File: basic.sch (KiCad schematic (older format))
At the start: 5 parts, among them J5 Conn_02x02_Top_Bottom, X1 dummy, X2 dummy

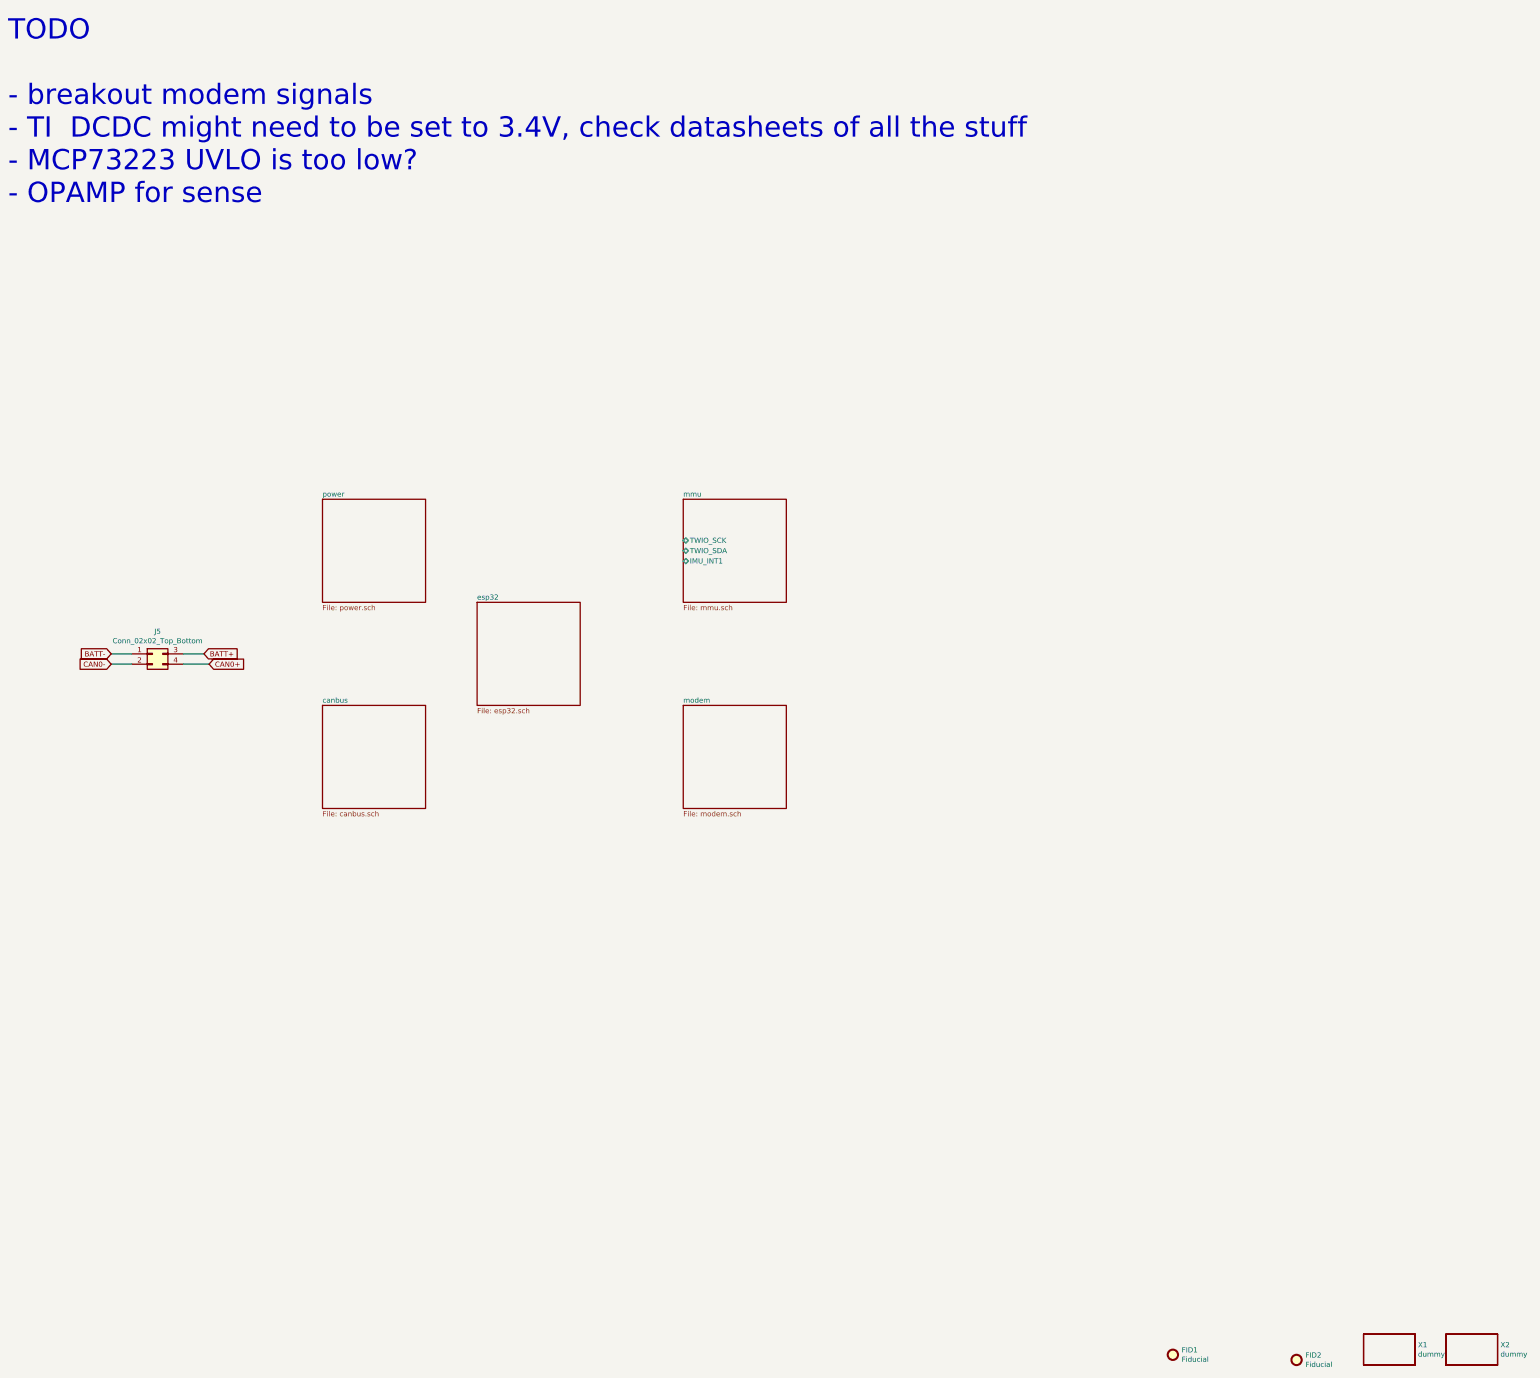
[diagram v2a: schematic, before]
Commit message: Esp32 & Canbus Sch. edited.
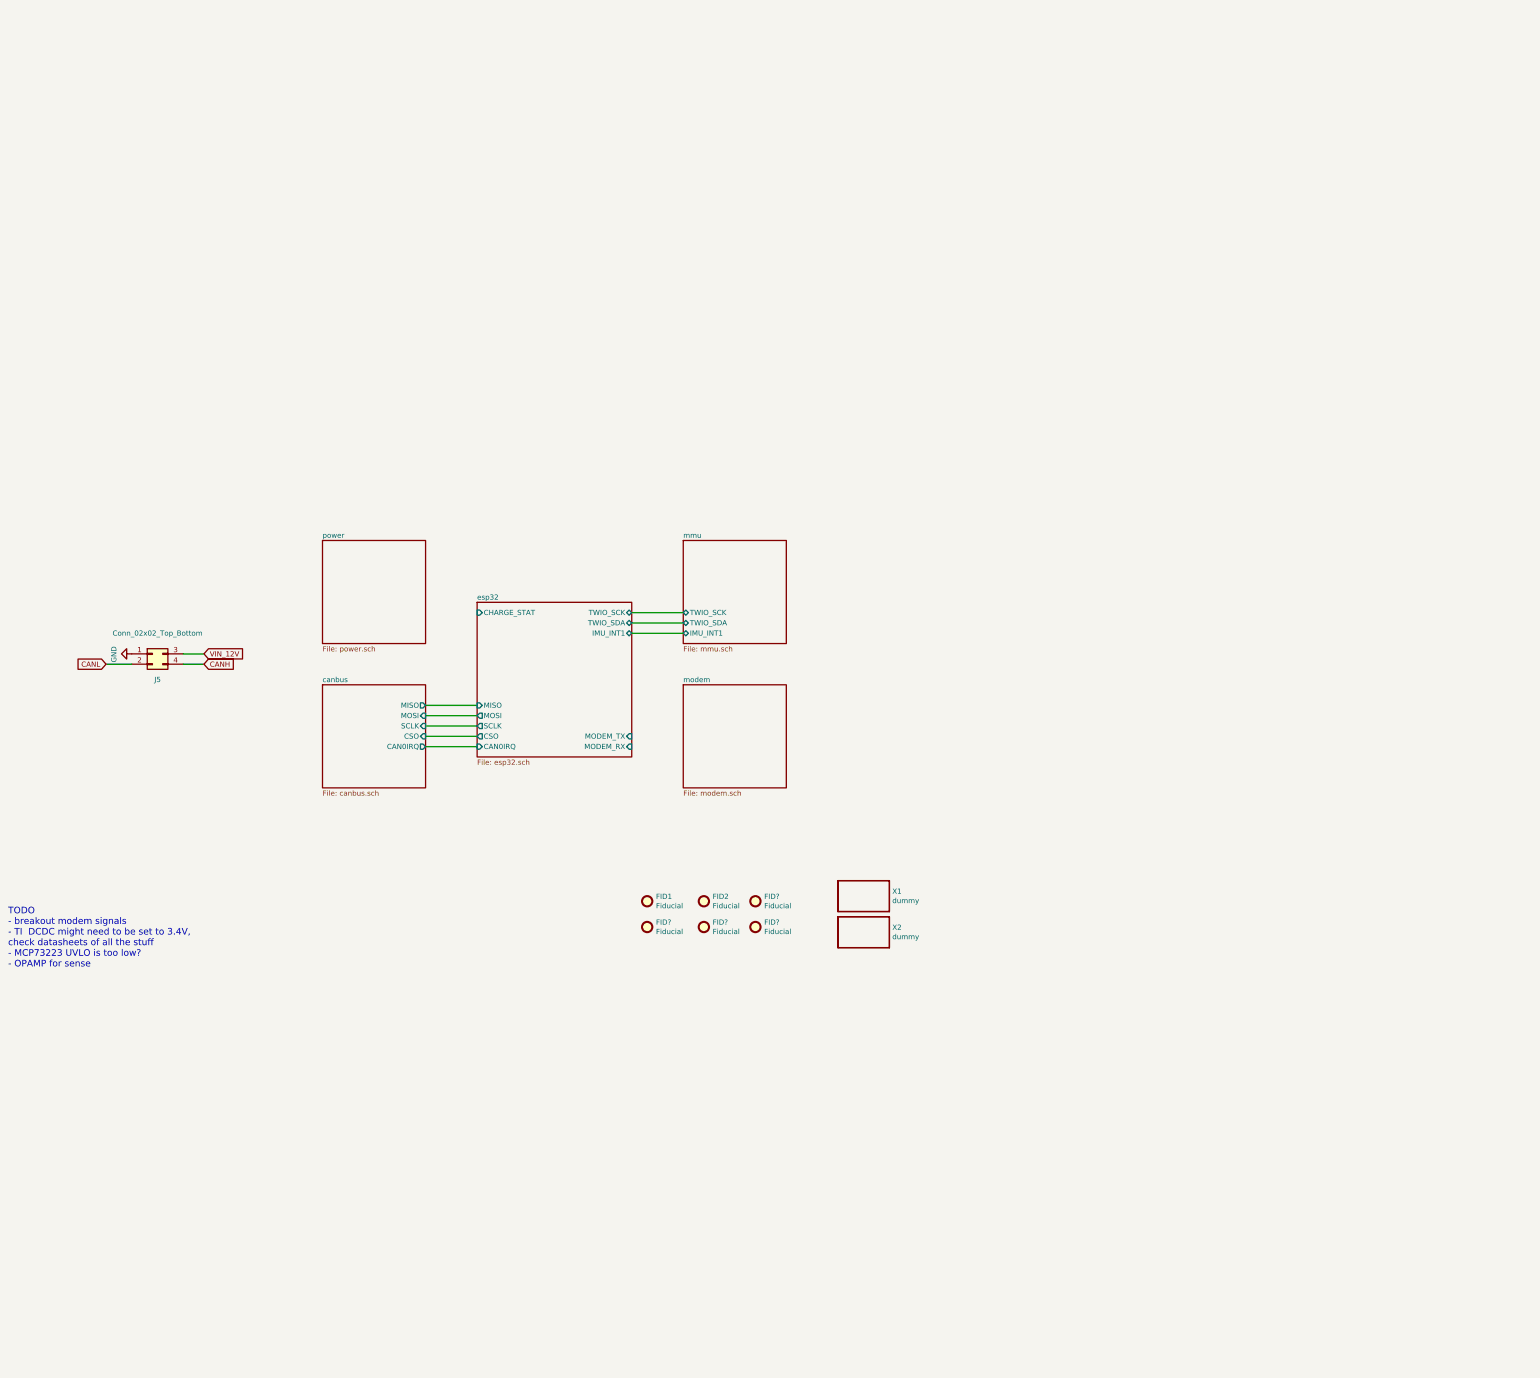
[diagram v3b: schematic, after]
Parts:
- added FID? (x4): Fiducial, Aesthetics:FIDUCIAL-1X2, symbol Mechanical:Fiducial
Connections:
- net BATT+ renamed VIN_12V
- net BATT- renamed GND
- net CAN0+ renamed CANH
- net CAN0- renamed CANL
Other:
- note added: "TODO\n- breakout modem signals\n- TI DCDC might need to be set to 3.4V, \ncheck datasheets of all the stuff\n- MCP73223 UVLO is too low?\n- OPAMP for sense"
- note removed: "TODO\n\n- breakout modem signals\n- TI DCDC might need to be set to 3.4V, check datasheets of all the stuff\n- MCP73223 UVLO is too low?\n- OPAMP for sense"
- moved on the sheet: FID1, FID2, X1, X2
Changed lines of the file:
@@
 L Mechanical:Fiducial FID1
 U 1 1 5E789BF2
-P 12250 10300
-F 0 "FID1" H 12335 10346 50  0000 L CNN
-F 1 "Fiducial" H 12335 10255 50  0000 L CNN
-F 2 "Aesthetics:FIDUCIAL-1X2" H 12250 10300 50  0001 C CNN
-F 3 "~" H 12250 10300 50  0001 C CNN
-	1    12250 10300
+P 7150 5900
+F 0 "FID1" H 7235 5946 50  0000 L CNN
+F 1 "Fiducial" H 7235 5855 50  0000 L CNN
+F 2 "Aesthetics:FIDUCIAL-1X2" H 7150 5900 50  0001 C CNN
+F 3 "~" H 7150 5900 50  0001 C CNN
+	1    7150 5900
 	1    0    0    -1
 $EndComp
 Wire Wire Line
 	2850 3500 2650 3500
-Wire Wire Line
-	1950 3600 2150 3600
-Text GLabel 2900 3600 2    50   Input ~ 0
-CAN0+
-Wire Wire Line
-	2650 3600 2900 3600
 $Comp
 L Mechanical:Fiducial FID2
 U 1 1 5E789C24
-P 13450 10350
-F 0 "FID2" H 13535 10396 50  0000 L CNN
-F 1 "Fiducial" H 13535 10305 50  0000 L CNN
-F 2 "Aesthetics:FIDUCIAL-1X2" H 13450 10350 50  0001 C CNN
-F 3 "~" H 13450 10350 50  0001 C CNN
-	1    13450 10350
+P 7700 5900
+F 0 "FID2" H 7785 5946 50  0000 L CNN
+F 1 "Fiducial" H 7785 5855 50  0000 L CNN
+F 2 "Aesthetics:FIDUCIAL-1X2" H 7700 5900 50  0001 C CNN
+F 3 "~" H 7700 5900 50  0001 C CNN
+	1    7700 5900
 	1    0    0    -1
 $EndComp
-Wire Wire Line
-	1950 3500 2150 3500
 Text GLabel 2850 3500 2    50   Input ~ 0
-BATT+
+VIN_12V
 $Comp
 L Connector_Generic:Conn_02x02_Top_Bottom J5
 U 1 1 5E789BF0
 P 2350 3500
-F 0 "J5" H 2400 3717 50  0000 C CNN
-F 1 "Conn_02x02_Top_Bottom" H 2400 3626 50  0000 C CNN
+F 0 "J5" H 2400 3250 50  0000 C CNN
+F 1 "Conn_02x02_Top_Bottom" H 2400 3700 50  0000 C CNN
 F 2 "Connector_Molex:Molex_Micro-Fit_3.0_43045-0400_2x02_P3.00mm_Horizontal" H 2350 3500 50  0001 C CNN
 F 3 "~" H 2350 3500 50  0001 C CNN
@@
 	1    0    0    -1
 $EndComp
-Text GLabel 1950 3500 0    50   Input ~ 0
-BATT-
-Text GLabel 1950 3600 0    50   Input ~ 0
-CAN0-
-Text Notes 950  -850 0    197  ~ 0
-TODO\n\n- breakout modem signals\n- TI  DCDC might need to be set to 3.4V, check datasheets of all the stuff\n- MCP73223 UVLO is too low?\n- OPAMP for sense
+Text Notes 950  6550 0    64   ~ 0
+TODO\n- breakout modem signals\n- TI  DCDC might need to be set to 3.4V, \ncheck datasheets of all the stuff\n- MCP73223 UVLO is too low?\n- OPAMP for sense
 $Sheet
-S 4000 2000 1000 1000
+S 4000 2400 1000 1000
 U 60856F71
 F0 "power" 50
@@
 L aep:dummy X1
 U 1 1 6202ADD4
-P 14350 10250
-F 0 "X1" H 14628 10296 50  0000 L CNN
-F 1 "dummy" H 14628 10205 50  0000 L CNN
-F 2 "aep:WEEE-Logo_2.1x3mm_SilkScreen" H 14350 10250 50  0001 C CNN
-F 3 "" H 14350 10250 50  0001 C CNN
-	1    14350 10250
+P 9250 5850
+F 0 "X1" H 9528 5896 50  0000 L CNN
+F 1 "dummy" H 9528 5805 50  0000 L CNN
+F 2 "aep:WEEE-Logo_2.1x3mm_SilkScreen" H 9250 5850 50  0001 C CNN
+F 3 "" H 9250 5850 50  0001 C CNN
+	1    9250 5850
 	1    0    0    -1
 $EndComp
@@
 L aep:dummy X2
 U 1 1 6202DDC3
-P 15150 10250
-F 0 "X2" H 15428 10296 50  0000 L CNN
-F 1 "dummy" H 15428 10205 50  0000 L CNN
-F 2 "Aesthetics:OSHW-LOGO-S" H 15150 10250 50  0001 C CNN
-F 3 "" H 15150 10250 50  0001 C CNN
-	1    15150 10250
+P 9250 6200
+F 0 "X2" H 9528 6246 50  0000 L CNN
+F 1 "dummy" H 9528 6155 50  0000 L CNN
+F 2 "Aesthetics:OSHW-LOGO-S" H 9250 6200 50  0001 C CNN
+F 3 "" H 9250 6200 50  0001 C CNN
+	1    9250 6200
 	1    0    0    -1
 $EndComp
 $Sheet
-S 4000 4000 1000 1000
+S 4000 3800 1000 1000
 U 603BB897
 F0 "canbus" 50
 F1 "canbus.sch" 50
+F2 "MISO" O R 5000 4000 50
+F3 "MOSI" I R 5000 4100 50
+F4 "SCLK" I R 5000 4200 50
+F5 "CSO" I R 5000 4300 50
+F6 "CAN0IRQ" O R 5000 4400 50
 $EndSheet
 $Sheet
-S 7500 4000 1000 1000
+S 7500 3800 1000 1000
 U 6055B0F2
 F0 "modem" 50
@@
 $EndSheet
 $Sheet
-S 7500 2000 1000 1000
+S 7500 2400 1000 1000
 U 606146CD
 F0 "mmu" 50
 F1 "mmu.sch" 50
-F2 "TWIO_SCK" B L 7500 2400 50
-F3 "TWIO_SDA" B L 7500 2500 50
-F4 "IMU_INT1" B L 7500 2600 50
+F2 "TWIO_SCK" B L 7500 3100 50
+F3 "TWIO_SDA" B L 7500 3200 50
+F4 "IMU_INT1" B L 7500 3300 50
 $EndSheet
+Wire Wire Line
+	7000 3100 7500 3100
+Wire Wire Line
+	7000 3200 7500 3200
+Wire Wire Line
+	7000 3300 7500 3300
+Wire Wire Line
+	5500 4000 5000 4000
+Wire Wire Line
+	5000 4100 5500 4100
+Wire Wire Line
+	5500 4200 5000 4200
+Wire Wire Line
+	5000 4300 5500 4300
+Wire Wire Line
+	5500 4400 5000 4400
+Text GLabel 2850 3600 2    50   Input ~ 0
+CANH
+Text GLabel 1900 3600 0    50   Input ~ 0
+CANL
+Wire Wire Line
+	2850 3600 2650 3600
 $Sheet
-S 5500 3000 1000 1000
+S 5500 3000 1500 1500
 U 603B75FA
 F0 "esp32" 50
 F1 "esp32.sch" 50
+F2 "TWIO_SCK" B R 7000 3100 50
+F3 "TWIO_SDA" B R 7000 3200 50
+F4 "IMU_INT1" B R 7000 3300 50
+F5 "MODEM_TX" I R 7000 4300 50
+F6 "MODEM_RX" I R 7000 4400 50
+F7 "CHARGE_STAT" I L 5500 3100 50
+F8 "CAN0IRQ" I L 5500 4400 50
+F9 "MISO" I L 5500 4000 50
+F10 "MOSI" O L 5500 4100 50
+F11 "SCLK" O L 5500 4200 50
+F12 "CSO" O L 5500 4300 50
 $EndSheet
+$Comp
+L Mechanical:Fiducial FID?
+U 1 1 605974C2
+P 8200 5900
+F 0 "FID?" H 8285 5946 50  0000 L CNN
+F 1 "Fiducial" H 8285 5855 50  0000 L CNN
+F 2 "Aesthetics:FIDUCIAL-1X2" H 8200 5900 50  0001 C CNN
+F 3 "~" H 8200 5900 50  0001 C CNN
+	1    8200 5900
+	1    0    0    -1
+$EndComp
+$Comp
+L Mechanical:Fiducial FID?
+U 1 1 60597847
+P 7150 6150
+F 0 "FID?" H 7235 6196 50  0000 L CNN
+F 1 "Fiducial" H 7235 6105 50  0000 L CNN
+F 2 "Aesthetics:FIDUCIAL-1X2" H 7150 6150 50  0001 C CNN
+F 3 "~" H 7150 6150 50  0001 C CNN
+	1    7150 6150
+	1    0    0    -1
+$EndComp
+$Comp
+L Mechanical:Fiducial FID?
+U 1 1 60597BC6
+P 7700 6150
+F 0 "FID?" H 7785 6196 50  0000 L CNN
+F 1 "Fiducial" H 7785 6105 50  0000 L CNN
+F 2 "Aesthetics:FIDUCIAL-1X2" H 7700 6150 50  0001 C CNN
+F 3 "~" H 7700 6150 50  0001 C CNN
+	1    7700 6150
+	1    0    0    -1
+$EndComp
+$Comp
+L Mechanical:Fiducial FID?
+U 1 1 60597F21
+P 8200 6150
+F 0 "FID?" H 8285 6196 50  0000 L CNN
+F 1 "Fiducial" H 8285 6105 50  0000 L CNN
+F 2 "Aesthetics:FIDUCIAL-1X2" H 8200 6150 50  0001 C CNN
+F 3 "~" H 8200 6150 50  0001 C CNN
+	1    8200 6150
+	1    0    0    -1
+$EndComp
+$Comp
+L power:GND #PWR?
+U 1 1 6059A4E7
+P 2150 3500
+AR Path="/603BB897/6059A4E7" Ref="#PWR?"  Part="1"
+AR Path="/6059A4E7" Ref="#PWR?"  Part="1"
+F 0 "#PWR?" H 2150 3250 50  0001 C CNN
+F 1 "GND" H 2155 3327 50  0000 C CNN
+F 2 "" H 2150 3500 50  0001 C CNN
+F 3 "" H 2150 3500 50  0001 C CNN
+	1    2150 3500
+	0    1    1    0
+$EndComp
+Wire Wire Line
+	1900 3600 2150 3600
 $EndSCHEMATC

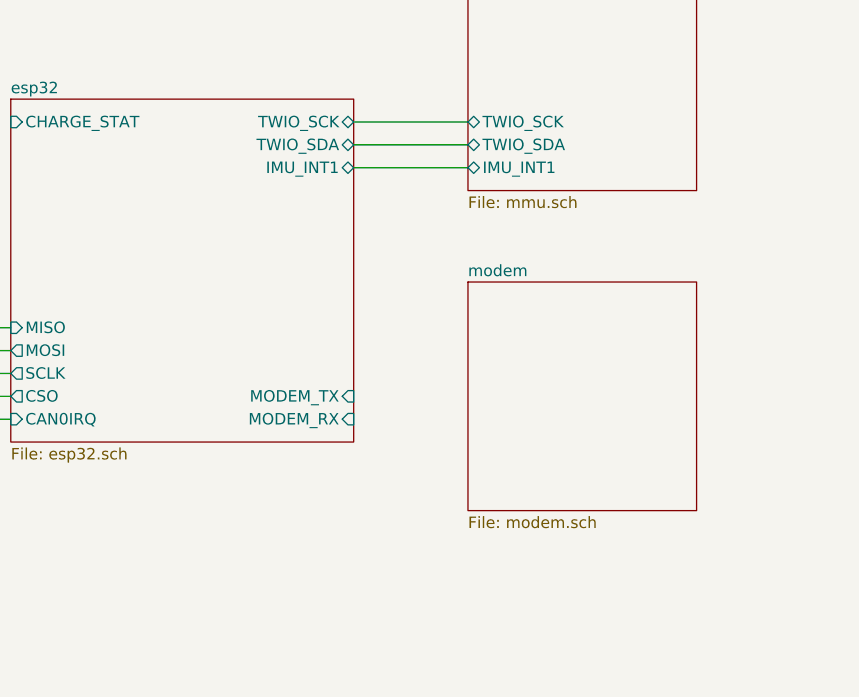
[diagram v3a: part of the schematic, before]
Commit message: Modem schematic updated.
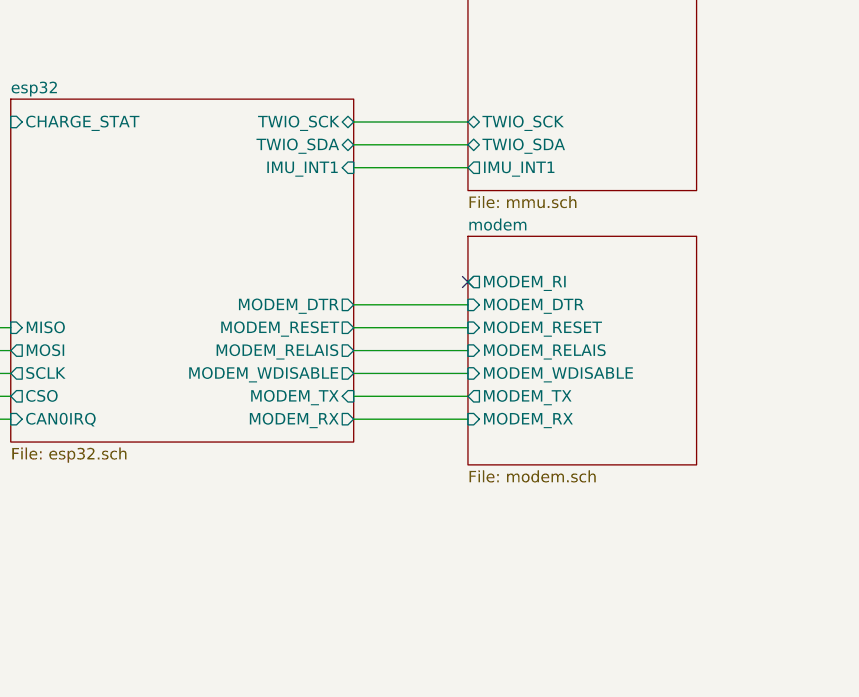
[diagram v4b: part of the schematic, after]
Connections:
- no-connect marks 0 -> 1
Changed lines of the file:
@@
-$EndSheet
-$Sheet
-S 7500 3800 1000 1000
-U 6055B0F2
-F0 "modem" 50
-F1 "modem.sch" 50
 $EndSheet
 $Sheet
@@
 F2 "TWIO_SCK" B L 7500 3100 50
 F3 "TWIO_SDA" B L 7500 3200 50
-F4 "IMU_INT1" B L 7500 3300 50
+F4 "IMU_INT1" O L 7500 3300 50
 $EndSheet
 Wire Wire Line
@@
 F2 "TWIO_SCK" B R 7000 3100 50
 F3 "TWIO_SDA" B R 7000 3200 50
-F4 "IMU_INT1" B R 7000 3300 50
-F5 "MODEM_TX" I R 7000 4300 50
-F6 "MODEM_RX" I R 7000 4400 50
-F7 "CHARGE_STAT" I L 5500 3100 50
-F8 "CAN0IRQ" I L 5500 4400 50
-F9 "MISO" I L 5500 4000 50
-F10 "MOSI" O L 5500 4100 50
-F11 "SCLK" O L 5500 4200 50
-F12 "CSO" O L 5500 4300 50
+F4 "CHARGE_STAT" I L 5500 3100 50
+F5 "CAN0IRQ" I L 5500 4400 50
+F6 "MISO" I L 5500 4000 50
+F7 "MOSI" O L 5500 4100 50
+F8 "SCLK" O L 5500 4200 50
+F9 "CSO" O L 5500 4300 50
+F10 "MODEM_TX" I R 7000 4300 50
+F11 "MODEM_RX" O R 7000 4400 50
+F12 "MODEM_RELAIS" O R 7000 4100 50
+F13 "MODEM_DTR" O R 7000 3900 50
+F14 "MODEM_WDISABLE" O R 7000 4200 50
+F15 "MODEM_RESET" O R 7000 4000 50
+F16 "IMU_INT1" I R 7000 3300 50
 $EndSheet
 $Comp
@@
 Wire Wire Line
 	1900 3600 2150 3600
+$Sheet
+S 7500 3600 1000 1000
+U 6055B0F2
+F0 "modem" 50
+F1 "modem.sch" 50
+F2 "MODEM_RX" I L 7500 4400 50
+F3 "MODEM_TX" O L 7500 4300 50
+F4 "MODEM_WDISABLE" I L 7500 4200 50
+F5 "MODEM_RESET" I L 7500 4000 50
+F6 "MODEM_RI" O L 7500 3800 50
+F7 "MODEM_DTR" I L 7500 3900 50
+F8 "MODEM_RELAIS" I L 7500 4100 50
+$EndSheet
+NoConn ~ 7500 3800
+Wire Wire Line
+	7000 3900 7500 3900
+Wire Wire Line
+	7000 4000 7500 4000
+Wire Wire Line
+	7000 4100 7500 4100
+Wire Wire Line
+	7000 4200 7500 4200
+Wire Wire Line
+	7000 4300 7500 4300
+Wire Wire Line
+	7000 4400 7500 4400
 $EndSCHEMATC
